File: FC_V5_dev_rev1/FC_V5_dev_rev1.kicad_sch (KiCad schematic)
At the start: 82 parts, among them IC2 AZ1117CH-3.3TRG1, IC3 RV-3028-C7_32.768kHz_1ppm_TA_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, J1 Conn_ARM_JTAG_SWD_10, J11 Conn_Coaxial, J12 USB_C_Receptacle_USB2.0_16P, J16 DEBUG, J3 Life Makes Lemonade, J4 Molex 503398-1892, J5 BM04B-SRSS-TB(LF)(SN), J6 Conn_Coaxial, J9 BM04B-SRSS-TB(LF)(SN), SW1 KMR2, SW2 KMR2, SW3 SW_Push_SPDT, U12 TCA9548ARGERQ1, U16 MCP9808T-E/MS, U2 E22-400M30S, U3 RP2350B, U4 RFM98PW, U5 RFM9xBreakout, U6 W25Q128JV, U7 LSM6DSOTR, U8 LSM303AGRTR

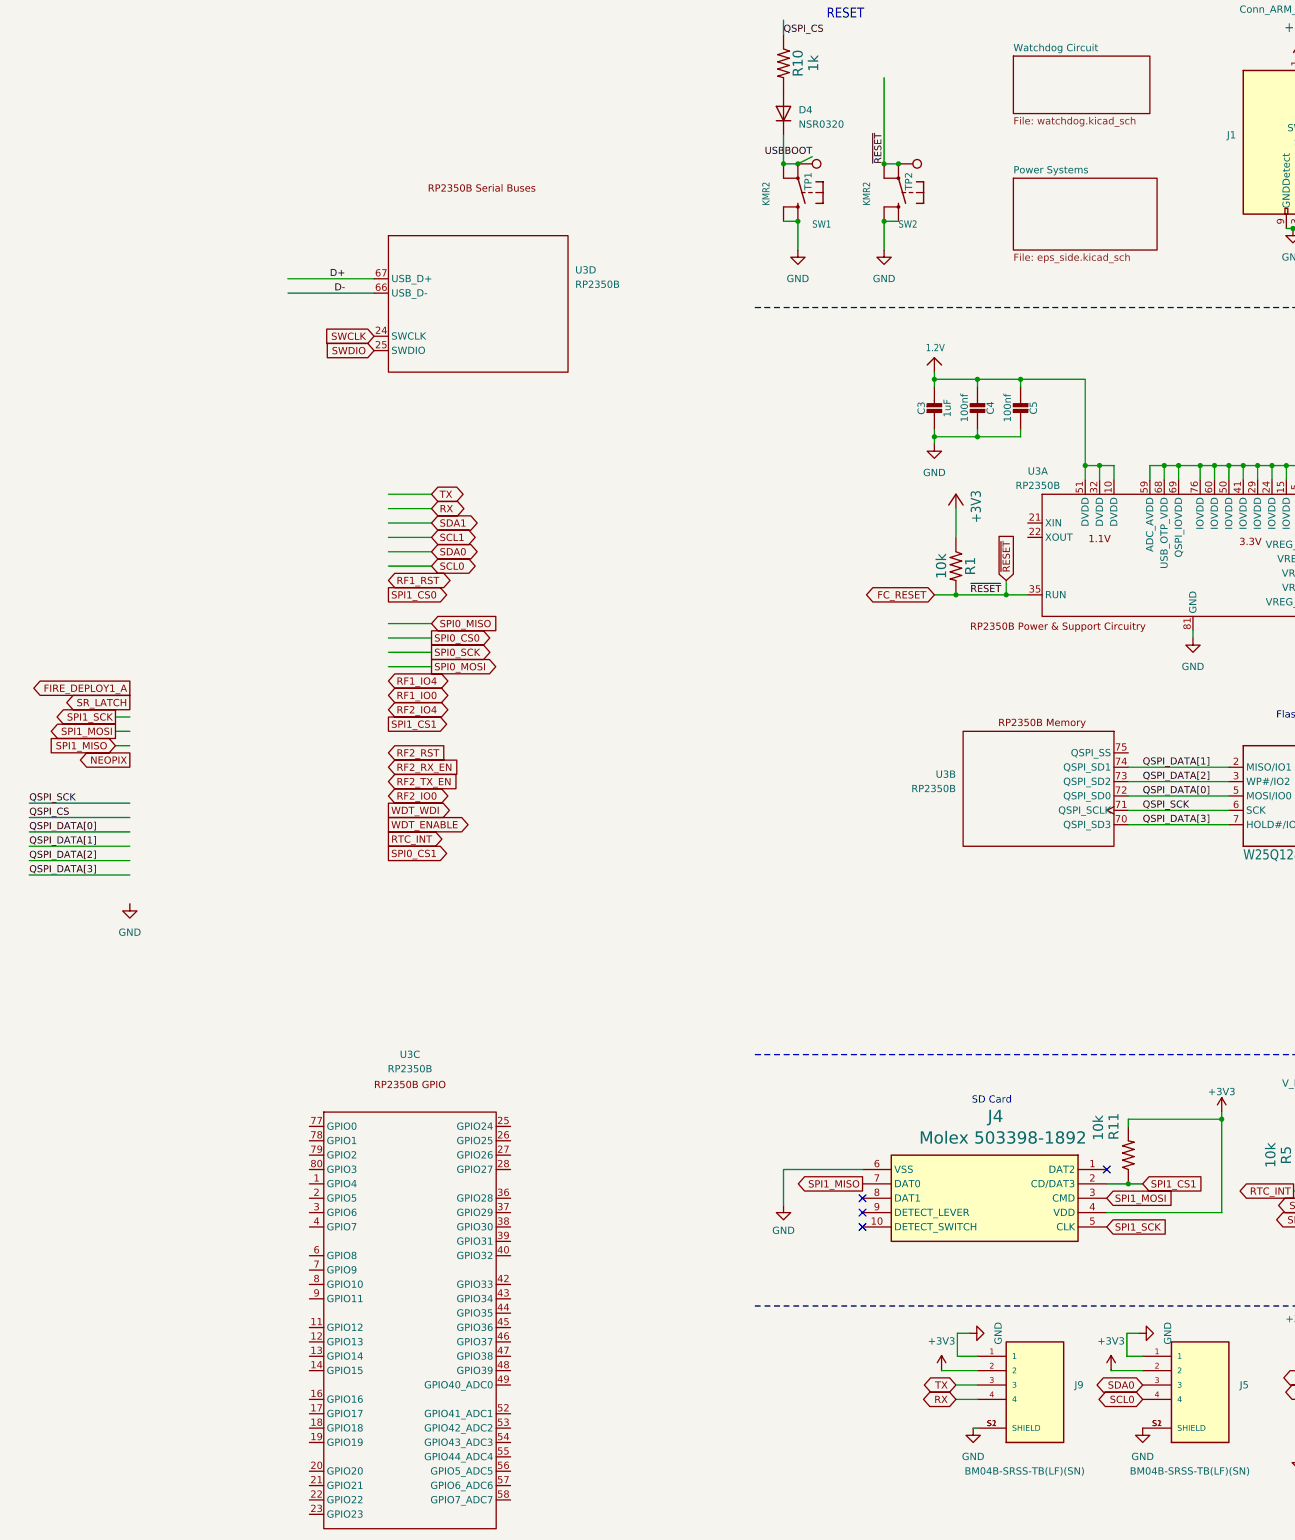
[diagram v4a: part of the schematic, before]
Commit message: Initial Setup of Serial Buses
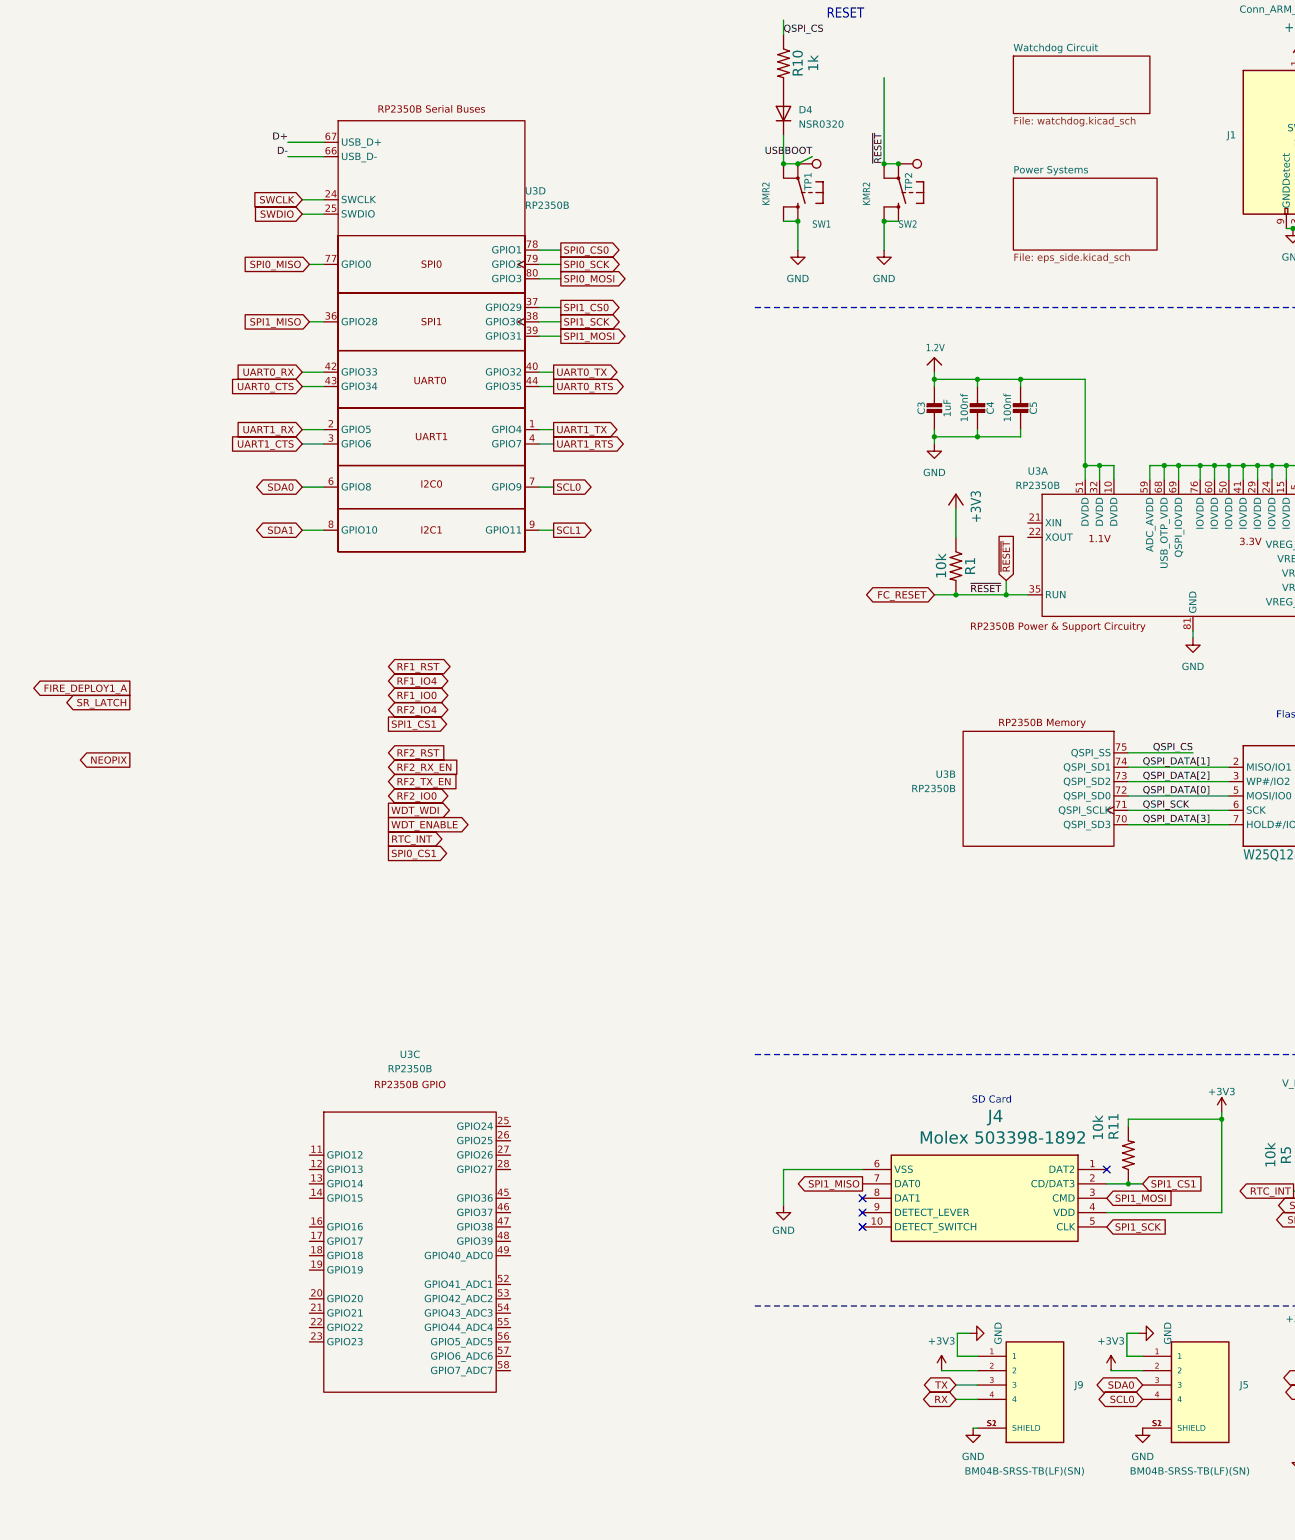
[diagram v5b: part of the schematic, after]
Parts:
- U3: Application Notes (none) -> https://datasheets.raspberrypi.com/rp2350/hardware-design-w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
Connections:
- net QSPI_CS: now also U3.75 (QSPI_SS)
- net SCL0: now also U3.7 (GPIO9)
- net SCL1: now also U3.9 (GPIO11)
- net SDA0: now also U3.6 (GPIO8)
- net SDA1: now also U3.8 (GPIO10)
- net SPI0_CS0: now also U3.78 (GPIO1)
- net SPI0_MISO: now also U3.77 (GPIO0)
- net SPI0_MOSI: now also U3.80 (GPIO3)
- net SPI0_SCK: now also U3.79 (GPIO2)
- net SPI1_CS0: now also U3.37 (GPIO29)
- net SPI1_MISO: now also U3.36 (GPIO28)
- net SPI1_MOSI: now also U3.39 (GPIO31)
- net SPI1_SCK: now also U3.38 (GPIO30)
- new net UART0_CTS: U3.43 (GPIO34)
- new net UART0_RTS: U3.44 (GPIO35)
- new net UART0_RX: U3.42 (GPIO33)
- new net UART0_TX: U3.40 (GPIO32)
- new net UART1_CTS: U3.3 (GPIO6)
- new net UART1_RTS: U3.4 (GPIO7)
- new net UART1_RX: U3.2 (GPIO5)
- new net UART1_TX: U3.1 (GPIO4)

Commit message: Reorganized Schematic
Now with more sheets than ever!
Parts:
- removed C10, C11, C17, C18, C32, C33, C34, C35, C4, C5, C7, C9: 100nf, Capacitor_SMD:C_0402_1005Metric, symbol Adafruit ItsyBitsy RP2040-eagle-import:CAP_CERAMIC_0402NO
- removed C14: 10uF, Capacitor_SMD:C_0603_1608Metric, symbol Device:C_Small
- removed C3: 1uF, Capacitor_SMD:C_0603_1608Metric, symbol Adafruit ItsyBitsy RP2040-eagle-import:CAP_CERAMIC_0603MP
- removed C31: 220nf, Capacitor_SMD:C_0402_1005Metric, symbol Adafruit ItsyBitsy RP2040-eagle-import:CAP_CERAMIC_0402NO
- removed C43: 1uF, Capacitor_SMD:C_0805_2012Metric, symbol Device:C
- removed C54, C56, C57, C58: 4.7uF, Capacitor_SMD:C_0402_1005Metric, symbol Adafruit ItsyBitsy RP2040-eagle-import:CAP_CERAMIC_0603MP
- removed C6, C8: 1uF, Capacitor_SMD:C_0402_1005Metric, symbol Adafruit ItsyBitsy RP2040-eagle-import:CAP_CERAMIC_0603MP
- removed D1, D2, D3: LED, LED_SMD:LED_0603_1608Metric, symbol Device:LED
- removed D4: NSR0320, Diode_SMD:D_SOD-323F, symbol Diode:1SS355VM
- removed IC3: RV-3028-C7_32.768kHz_1ppm_TA_QC, RTC:RV3028C7, symbol RV-3028-C7:RV-3028-C7_32.768kHz_1ppm_TA_QC
- removed J1: Conn_ARM_JTAG_SWD_10, FC_DEV_BOARD:JTAG_2X05_1.27MM_BOX_NOCREAM, symbol Connector:Conn_ARM_JTAG_SWD_10
- removed J11, J6: Conn_Coaxial, Connector_Coaxial:SMA_Amphenol_901-144_Vertical, symbol Connector:Conn_Coaxial
- removed J12: USB_C_Receptacle_USB2.0_16P, Connector_USB:USB_C_Receptacle_HRO_TYPE-C-31-M-12, symbol Connector:USB_C_Receptacle_USB2.0_16P
- removed J4: Molex 503398-1892, 503398-1892-1, symbol Molex 503398-1892:503398-1892
- removed JP10: Jumper_3_Open, Jumper:SolderJumper-3_P1.3mm_Open_RoundedPad1.0x1.5mm_NumberLabels, symbol Jumper:Jumper_3_Open
- removed JP11: SolderJumper_2_Open, Jumper:SolderJumper-2_P1.3mm_Open_RoundedPad1.0x1.5mm, symbol Jumper:SolderJumper_2_Open
- removed L3: L, symbol Device:L
- removed LED1: WS2812B_SK6812_1515, LED_SMD:LED_WS2812B_PLCC4_5.0x5.0mm_P3.2mm, symbol Adafruit ItsyBitsy RP2040-eagle-import:WS2812B_SK6805_1515
- removed R1, R11, R12, R14, R5, R9: 10k, Resistor_SMD:R_0603_1608Metric, symbol mainboard:RESISTOR0603
- removed R10, R3, R4: 1k, Resistor_SMD:R_0603_1608Metric, symbol mainboard:RESISTOR0603
- removed R13: 10k, Resistor_SMD:R_0603_1608Metric, symbol mainboard:10KOHM-1_10W-1%(0603)0603
- removed R15: 10K, Resistor_SMD:R_0603_1608Metric, symbol Device:R_US
- removed R24: 33, Resistor_SMD:R_0603_1608Metric, symbol mainboard:RESISTOR0603
- removed R25, R39, R45, R6: 10k, Resistor_SMD:R_Array_Convex_4x0603, symbol Device:R_Pack04
- removed R26, R27: 5.1k, Resistor_SMD:R_0603_1608Metric, symbol mainboard:RESISTOR0603
- removed R7, R8: 22, Resistor_SMD:R_0603_1608Metric, symbol mainboard:RESISTOR0603
- removed SW1, SW2: KMR2, FC_DEV_BOARD:BTN_KMR2_4.6X2.8, symbol Adafruit ItsyBitsy RP2040-eagle-import:SWITCH_TACT_SMT4.6X2.8
- removed TP1: USBBOOT, TestPoint:TestPoint_Loop_D1.80mm_Drill1.0mm_Beaded, symbol Connector:TestPoint
- removed TP2, TP6, TP7, TP8: RESET, TestPoint:TestPoint_Loop_D1.80mm_Drill1.0mm_Beaded, symbol Connector:TestPoint
- removed U12: TCA9548ARGERQ1, TCAQ1:QFN_GERQ1_TEX, symbol TCA9548ARGERQ1:TCA9548ARGERQ1
- removed U16: MCP9808T-E/MS, Package_SO:MSOP-8-1EP_3x3mm_P0.65mm_EP1.5x1.8mm_ThermalVias, symbol Sensor_Temperature:MCP9808_DFN
- removed U2: E22-400M30S, E22-400M30S:E22-400M30S, symbol RF_Module:E22-400M30S
- removed U3: RP2350B, RP2350:QFN-80_L10.0-W10.0-P0.40-TL-EP3.4, symbol PROVES:RP2350B
- removed U4: RFM98PW, FC_DEV_BOARD:RFM98PW, symbol mainboard:RFM98PW
- removed U5: RFM9xBreakout, RF_Module:HOPERF_RFM9XW_SMD, symbol mainboard:RFM9xBreakout
- removed U6: W25Q128JV, Package_SO:SOIC-8_5.275x5.275mm_P1.27mm, symbol Adafruit ItsyBitsy RP2040-eagle-import:SPIFLASH_8PIN_4X4
- removed U7: LSM6DSOTR, Package_LGA:LGA-14_3x2.5mm_P0.5mm_LayoutBorder3x4y, symbol LSM6DSOTR:LSM6DSOTR
- removed U8: LSM303AGRTR, Package_LGA:LGA-12_2x2mm_P0.5mm, symbol LSM303AGTR:LSM303AGRTR
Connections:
- no-connect marks 36 -> 1
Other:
- added sheet Onboard Sensors (sensors.kicad_sch)
- added sheet RP2350 (RP2350B_Core.kicad_sch)
- added sheet Radios (radios.kicad_sch)
- note removed: "Flash Memory"
- note removed: "IMU"
- note removed: "Modular Radios (HopeRF format)"
- note removed: "RESET"
- note removed: "Radio #1"
- note removed: "SD Card"
- note removed: "Sensor Multiplexer"
- note removed: "Temperature Sensor"
- moved on the sheet: C12, C13, H1, H2, IC2, J16, J3, J5, J9, SW3

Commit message: Return of the Shift Register
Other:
- added sheet Face Interface (face_interface.kicad_sch)
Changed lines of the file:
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@@
+	)
+	(sheet
+		(at 182.88 73.66)
+		(size 30.48 15.24)
+		(exclude_from_sim no)
+		(in_bom yes)
+		(on_board yes)
+		(dnp no)
+		(fields_autoplaced yes)
+		(stroke
+			(width 0.1524)
+			(type solid)
+		)
+		(fill
+			(color 0 0 0 0.0000)
+		)
+		(property "Sheetname" "Face Interface"
+			(at 182.88 72.9484 0)
+			(effects
+				(font
+					(size 1.27 1.27)
+				)
+				(justify left bottom)
+			)
+		)
+		(property "Sheetfile" "face_interface.kicad_sch"
+			(at 182.88 89.4846 0)
+			(effects
+				(font
+					(size 1.27 1.27)
+				)
+				(justify left top)
+			)
+		)
+		(instances
+			(project "FC_V5_dev_rev1"
+				(path "/c64c0d72-a9f6-4f3a-891e-1f647558f538"
+					(page "9")
+				)
+			)
+		)
 	)
 	(sheet
@@
 	)
 	(sheet
-		(at 100.33 66.04)
+		(at 96.52 69.85)
 		(size 34.29 16.51)
 		(exclude_from_sim no)
@@
 		)
 		(property "Sheetname" "RP2350"
-			(at 100.33 65.3284 0)
+			(at 96.52 69.1384 0)
 			(effects
 				(font
@@
 		)
 		(property "Sheetfile" "RP2350B_Core.kicad_sch"
-			(at 100.33 83.1346 0)
+			(at 96.52 86.9446 0)
 			(effects
 				(font
